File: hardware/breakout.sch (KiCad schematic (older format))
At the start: 4 parts, among them J1 Conn_01x18_Male, J2 Conn_Coaxial, J3 Conn_01x18_Male, U1 RFM95W-915S2

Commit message: Create pcb
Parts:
- added J4: Conn_Coaxial, KiCad/kicad-footprints/Connector_Coaxial.pretty:U.FL_Molex_MCRF_73412-0110_Vertical, symbol Connector:Conn_Coaxial
- added JP1: SolderJumper, KiCad/kicad-footprints/Jumper.pretty:SolderJumper-3_P1.3mm_Open_RoundedPad1.0x1.5mm, symbol Jumper:SolderJumper_3_Open
- J1, J3: footprint (none) -> KiCad/kicad-footprints/Connector_PinHeader_2.54mm.pretty:PinHeader_1x18_P2.54mm_Vertical
- J2: footprint (none) -> KiCad/kicad-footprints/Connector_Coaxial.pretty:SMA_Amphenol_132289_EdgeMount
- U1: footprint (none) -> KiCad/kicad-footprints/RF_Module.pretty:HOPERF_RFM9XW_SMD
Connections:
- net GND: now also J2.2 (Ext), J4.2 (Ext)
- net DIO0: now reaches J3.8 (Pin_8)
- net DIO0: now also U1.14 (DIO0); no longer U1.11 (DIO3)
- net DIO3: now reaches J3.7 (Pin_7)
- net DIO3: now also U1.11 (DIO3); no longer U1.14 (DIO0)
- net at U1.5 (NSS): now also J1.9 (Pin_9)
- net at U1.9 (ANT): now also JP1.2 (C); no longer J2.2 (Ext)
- net at J2.1 (In): now also JP1.1 (A)
- new net: J4.1 (In), JP1.3 (B)
- no-connect marks 28 -> 31
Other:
- moved on the sheet: J2
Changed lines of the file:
@@
 encoding utf-8
 Sheet 1 1
-Title ""
-Date ""
-Rev ""
-Comp ""
+Title "RFM95 Breakout board for Zolertia RE-Mote rev-b"
+Date "2020-10-09"
+Rev "0"
+Comp "Thomas Perale"
 Comment1 ""
 Comment2 ""
@@
 F 0 "U1" H 5900 3950 50  0000 C CNN
 F 1 "RFM95W-915S2" H 6350 3400 50  0000 C CNN
-F 2 "" H 2600 5600 50  0001 C CNN
+F 2 "KiCad/kicad-footprints/RF_Module.pretty:HOPERF_RFM9XW_SMD" H 2600 5600 50  0001 C CNN
 F 3 "https://www.hoperf.com/data/upload/portal/20181127/5bfcbea20e9ef.pdf" H 2600 5600 50  0001 C CNN
 	1    5900 3950
@@
 L Connector:Conn_Coaxial J2
 U 1 1 5F7F506A
-P 6800 2550
-F 0 "J2" H 6900 2525 50  0000 L CNN
-F 1 "Conn_Coaxial" H 6900 2434 50  0000 L CNN
-F 2 "" H 6800 2550 50  0001 C CNN
-F 3 " ~" H 6800 2550 50  0001 C CNN
-	1    6800 2550
-	1    0    0    -1
+P 6150 2800
+F 0 "J2" H 6250 2775 50  0000 L CNN
+F 1 "Conn_Coaxial" H 5600 2500 50  0000 L CNN
+F 2 "KiCad/kicad-footprints/Connector_Coaxial.pretty:SMA_Amphenol_132289_EdgeMount" H 6150 2800 50  0001 C CNN
+F 3 " ~" H 6150 2800 50  0001 C CNN
+	1    6150 2800
+	-1   0    0    1
 $EndComp
 Wire Wire Line
@@
 P 5900 3200
 F 0 "#PWR03" H 5900 3050 50  0001 C CNN
-F 1 "+3.3V" H 5915 3373 50  0000 C CNN
+F 1 "+3.3V" H 5750 3200 50  0000 C CNN
 F 2 "" H 5900 3200 50  0001 C CNN
 F 3 "" H 5900 3200 50  0001 C CNN
@@
 Wire Wire Line
 	5900 3200 5900 3450
-Wire Wire Line
-	6400 3650 6800 3650
-Wire Wire Line
-	6800 3650 6800 2750
 Wire Wire Line
 	4350 4850 4650 4850
@@
 F 0 "J1" H 4258 4931 50  0000 C CNN
 F 1 "Conn_01x18_Male" H 4150 2900 50  0000 C CNN
-F 2 "" H 4150 3950 50  0001 C CNN
+F 2 "KiCad/kicad-footprints/Connector_PinHeader_2.54mm.pretty:PinHeader_1x18_P2.54mm_Vertical" H 4150 3950 50  0001 C CNN
 F 3 "~" H 4150 3950 50  0001 C CNN
 	1    4150 3950
@@
 NoConn ~ 4350 3750
 NoConn ~ 4350 3850
-NoConn ~ 4350 3950
 NoConn ~ 4350 4050
 NoConn ~ 4350 4150
@@
 F 0 "J3" H 7672 3932 50  0000 R CNN
 F 1 "Conn_01x18_Male" H 8000 5000 50  0000 R CNN
-F 2 "" H 7700 4050 50  0001 C CNN
+F 2 "KiCad/kicad-footprints/Connector_PinHeader_2.54mm.pretty:PinHeader_1x18_P2.54mm_Vertical" H 7700 4050 50  0001 C CNN
 F 3 "~" H 7700 4050 50  0001 C CNN
 	1    7700 4050
@@
 NoConn ~ 7500 4850
 NoConn ~ 7500 3250
-Wire Wire Line
-	7500 4150 6900 4150
-Wire Wire Line
-	6900 4150 6900 4050
-Wire Wire Line
-	6900 4050 6400 4050
-Wire Wire Line
-	6900 4250 6900 4350
-Wire Wire Line
-	6900 4350 6400 4350
-Wire Wire Line
-	6900 4250 7500 4250
+NoConn ~ 6400 3850
+NoConn ~ 6400 3950
+NoConn ~ 6400 4150
+NoConn ~ 6400 4250
+$Comp
+L power:GND #PWR0101
+U 1 1 5F81E473
+P 6150 2600
+F 0 "#PWR0101" H 6150 2350 50  0001 C CNN
+F 1 "GND" H 6250 2500 50  0000 C CNN
+F 2 "" H 6150 2600 50  0001 C CNN
+F 3 "" H 6150 2600 50  0001 C CNN
+	1    6150 2600
+	-1   0    0    1
+$EndComp
+Wire Wire Line
+	6400 3650 6550 3650
+Wire Wire Line
+	4350 3950 5400 3950
+Wire Wire Line
+	7500 4250 7350 4250
+Wire Wire Line
+	7500 4150 7350 4150
+Wire Wire Line
+	6400 4050 6650 4050
+Wire Wire Line
+	6400 4350 6650 4350
+Text Label 6650 4350 0    50   ~ 0
+DIO0
+Text Label 7350 4150 2    50   ~ 0
+DIO0
+Text Label 6650 4050 0    50   ~ 0
+DIO3
+Text Label 7350 4250 2    50   ~ 0
+DIO3
+$Comp
+L Connector:Conn_Coaxial J4
+U 1 1 5F844AB1
+P 6950 2800
+F 0 "J4" H 7050 2775 50  0000 L CNN
+F 1 "Conn_Coaxial" H 6950 2950 50  0000 L CNN
+F 2 "KiCad/kicad-footprints/Connector_Coaxial.pretty:U.FL_Molex_MCRF_73412-0110_Vertical" H 6950 2800 50  0001 C CNN
+F 3 " ~" H 6950 2800 50  0001 C CNN
+	1    6950 2800
+	1    0    0    -1
+$EndComp
+$Comp
+L power:GND #PWR0102
+U 1 1 5F8463B3
+P 6950 3000
+F 0 "#PWR0102" H 6950 2750 50  0001 C CNN
+F 1 "GND" H 7050 2900 50  0000 C CNN
+F 2 "" H 6950 3000 50  0001 C CNN
+F 3 "" H 6950 3000 50  0001 C CNN
+	1    6950 3000
+	1    0    0    -1
+$EndComp
+Wire Wire Line
+	6550 2950 6550 3650
+$Comp
+L Jumper:SolderJumper_3_Open JP1
+U 1 1 5F88236B
+P 6550 2800
+F 0 "JP1" H 6550 3005 50  0000 C CNN
+F 1 "SolderJumper" H 6550 2914 50  0000 C CNN
+F 2 "KiCad/kicad-footprints/Jumper.pretty:SolderJumper-3_P1.3mm_Open_RoundedPad1.0x1.5mm" H 6550 2800 50  0001 C CNN
+F 3 "~" H 6550 2800 50  0001 C CNN
+	1    6550 2800
+	1    0    0    -1
+$EndComp
 $EndSCHEMATC

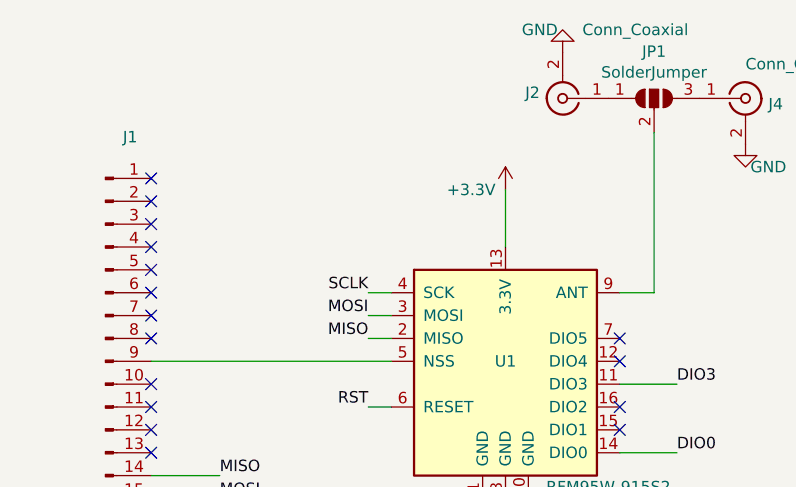
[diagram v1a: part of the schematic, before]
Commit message: [enh] The complete outline is overkill
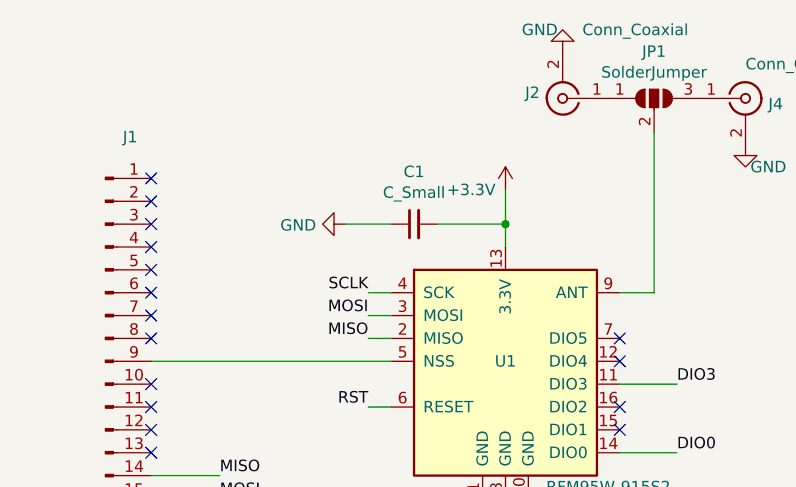
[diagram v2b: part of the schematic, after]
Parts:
- added C1: C_Small, Capacitor_SMD:C_1206_3216Metric_Pad1.33x1.80mm_HandSolder, symbol Device:C_Small
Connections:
- net +3V3: now also C1.2
- net GND: now also C1.1
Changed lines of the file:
@@
 $EndComp
 Wire Wire Line
-	5900 3200 5900 3450
+	5900 3200 5900 3350
 Wire Wire Line
 	4350 4850 4650 4850
@@
 	1    0    0    -1
 $EndComp
+Wire Wire Line
+	5900 3350 5600 3350
+Connection ~ 5900 3350
+Wire Wire Line
+	5900 3350 5900 3450
+$Comp
+L Device:C_Small C1
+U 1 1 5F8492C2
+P 5500 3350
+F 0 "C1" V 5729 3350 50  0000 C CNN
+F 1 "C_Small" V 5638 3350 50  0000 C CNN
+F 2 "Capacitor_SMD:C_1206_3216Metric_Pad1.33x1.80mm_HandSolder" H 5500 3350 50  0001 C CNN
+F 3 "~" H 5500 3350 50  0001 C CNN
+	1    5500 3350
+	0    -1   -1   0
+$EndComp
+Wire Wire Line
+	5400 3350 5200 3350
+$Comp
+L power:GND #PWR0103
+U 1 1 5F84AA53
+P 5200 3350
+F 0 "#PWR0103" H 5200 3100 50  0001 C CNN
+F 1 "GND" V 5205 3222 50  0000 R CNN
+F 2 "" H 5200 3350 50  0001 C CNN
+F 3 "" H 5200 3350 50  0001 C CNN
+	1    5200 3350
+	0    1    1    0
+$EndComp
 $EndSCHEMATC

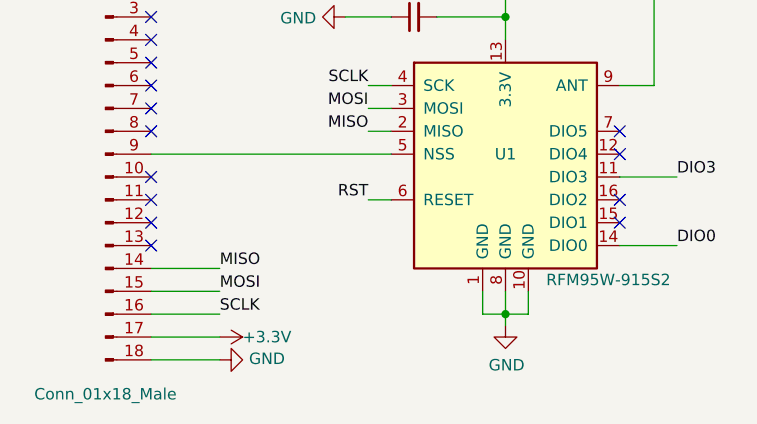
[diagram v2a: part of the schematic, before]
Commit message: [add] Push button for manual rseet
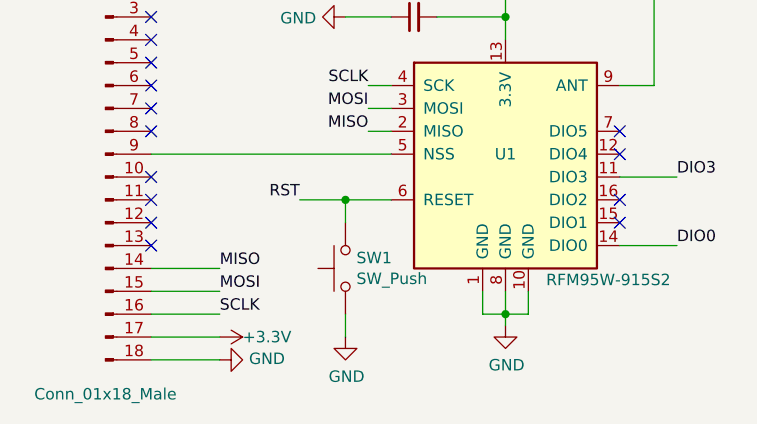
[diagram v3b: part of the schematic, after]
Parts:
- added SW1: SW_Push, KiCad/kicad-footprints/Button_Switch_SMD.pretty:SW_DIP_SPSTx01_Slide_6.7x4.1mm_W8.61mm_P2.54mm_LowProfile, symbol Switch:SW_Push
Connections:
- net GND: now also SW1.1
- net RST: now also SW1.2
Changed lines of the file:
@@
 Text Label 7350 3350 2    50   ~ 0
 RST
-Wire Wire Line
-	5400 4150 5300 4150
-Text Label 5300 4150 2    50   ~ 0
+Text Label 5000 4150 2    50   ~ 0
 RST
 $Comp
@@
 	0    1    1    0
 $EndComp
+Wire Wire Line
+	5000 4150 5200 4150
+Wire Wire Line
+	5200 4150 5200 4250
+Connection ~ 5200 4150
+Wire Wire Line
+	5200 4150 5400 4150
+$Comp
+L Switch:SW_Push SW1
+U 1 1 5F866186
+P 5200 4450
+F 0 "SW1" V 5246 4402 50  0000 R CNN
+F 1 "SW_Push" V 5155 4402 50  0000 R CNN
+F 2 "KiCad/kicad-footprints/Button_Switch_SMD.pretty:SW_DIP_SPSTx01_Slide_6.7x4.1mm_W8.61mm_P2.54mm_LowProfile" H 5200 4650 50  0001 C CNN
+F 3 "~" H 5200 4650 50  0001 C CNN
+	1    5200 4450
+	0    -1   -1   0
+$EndComp
+Wire Wire Line
+	5200 4650 5200 4750
+$Comp
+L power:GND #PWR0104
+U 1 1 5F867EB7
+P 5200 4750
+F 0 "#PWR0104" H 5200 4500 50  0001 C CNN
+F 1 "GND" H 5205 4577 50  0000 C CNN
+F 2 "" H 5200 4750 50  0001 C CNN
+F 3 "" H 5200 4750 50  0001 C CNN
+	1    5200 4750
+	1    0    0    -1
+$EndComp
 $EndSCHEMATC

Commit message: [add] Debouncing circuit
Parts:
- added C2: 1uF, Capacitor_SMD:C_1206_3216Metric_Pad1.33x1.80mm_HandSolder, symbol Device:C_Small
- added R1: 220R, Resistor_SMD:R_1206_3216Metric_Pad1.30x1.75mm_HandSolder, symbol Device:R_Small
- added R2: 10KR, Resistor_SMD:R_1206_3216Metric_Pad1.30x1.75mm_HandSolder, symbol Device:R_Small
- C1: value C_Small -> 10uF
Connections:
- net +3V3: now also R2.2
- net GND: now also C2.1
- net RST: now also C2.2, R1.2; no longer J3.16 (Pin_16), SW1.2
- new net RST_GPIO: J3.16 (Pin_16), R1.1, R2.1, SW1.2
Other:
- note added: "Reset Push Button"
- moved on the sheet: SW1
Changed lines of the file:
@@
 	7500 3350 7350 3350
 Text Label 7350 3350 2    50   ~ 0
-RST
-Text Label 5000 4150 2    50   ~ 0
+RST_GPIO
+Text Label 5300 4150 2    50   ~ 0
 RST
 $Comp
@@
 P 5500 3350
 F 0 "C1" V 5729 3350 50  0000 C CNN
-F 1 "C_Small" V 5638 3350 50  0000 C CNN
+F 1 "10uF" V 5638 3350 50  0000 C CNN
 F 2 "Capacitor_SMD:C_1206_3216Metric_Pad1.33x1.80mm_HandSolder" H 5500 3350 50  0001 C CNN
 F 3 "~" H 5500 3350 50  0001 C CNN
@@
 	0    1    1    0
 $EndComp
-Wire Wire Line
-	5000 4150 5200 4150
-Wire Wire Line
-	5200 4150 5200 4250
-Connection ~ 5200 4150
-Wire Wire Line
-	5200 4150 5400 4150
 $Comp
 L Switch:SW_Push SW1
 U 1 1 5F866186
-P 5200 4450
-F 0 "SW1" V 5246 4402 50  0000 R CNN
-F 1 "SW_Push" V 5155 4402 50  0000 R CNN
-F 2 "KiCad/kicad-footprints/Button_Switch_SMD.pretty:SW_DIP_SPSTx01_Slide_6.7x4.1mm_W8.61mm_P2.54mm_LowProfile" H 5200 4650 50  0001 C CNN
-F 3 "~" H 5200 4650 50  0001 C CNN
-	1    5200 4450
+P 2300 4300
+F 0 "SW1" V 2250 4250 50  0000 R CNN
+F 1 "SW_Push" V 2150 4250 50  0000 R CNN
+F 2 "KiCad/kicad-footprints/Button_Switch_SMD.pretty:SW_DIP_SPSTx01_Slide_6.7x4.1mm_W8.61mm_P2.54mm_LowProfile" H 2300 4500 50  0001 C CNN
+F 3 "~" H 2300 4500 50  0001 C CNN
+	1    2300 4300
 	0    -1   -1   0
 $EndComp
-Wire Wire Line
-	5200 4650 5200 4750
 $Comp
 L power:GND #PWR0104
 U 1 1 5F867EB7
-P 5200 4750
-F 0 "#PWR0104" H 5200 4500 50  0001 C CNN
-F 1 "GND" H 5205 4577 50  0000 C CNN
-F 2 "" H 5200 4750 50  0001 C CNN
-F 3 "" H 5200 4750 50  0001 C CNN
-	1    5200 4750
-	1    0    0    -1
-$EndComp
+P 2300 4800
+F 0 "#PWR0104" H 2300 4550 50  0001 C CNN
+F 1 "GND" H 2305 4627 50  0000 C CNN
+F 2 "" H 2300 4800 50  0001 C CNN
+F 3 "" H 2300 4800 50  0001 C CNN
+	1    2300 4800
+	1    0    0    -1
+$EndComp
+Wire Wire Line
+	2000 4000 2000 4200
+$Comp
+L Device:C_Small C2
+U 1 1 5F874ED2
+P 2000 4300
+F 0 "C2" H 1950 4400 50  0000 C CNN
+F 1 "1uF" H 1900 4500 50  0000 C CNN
+F 2 "Capacitor_SMD:C_1206_3216Metric_Pad1.33x1.80mm_HandSolder" H 2000 4300 50  0001 C CNN
+F 3 "~" H 2000 4300 50  0001 C CNN
+	1    2000 4300
+	-1   0    0    1
+$EndComp
+Wire Wire Line
+	2000 4400 2000 4650
+Wire Wire Line
+	2000 4650 2300 4650
+Wire Wire Line
+	5300 4150 5400 4150
+Wire Wire Line
+	2300 4500 2300 4650
+Connection ~ 2300 4650
+Wire Wire Line
+	2300 4650 2300 4800
+Wire Wire Line
+	2300 4100 2300 4000
+Wire Wire Line
+	2300 4000 2550 4000
+$Comp
+L Device:R_Small R1
+U 1 1 5F8A20C0
+P 2150 4000
+F 0 "R1" V 1954 4000 50  0000 C CNN
+F 1 "220R" V 2045 4000 50  0000 C CNN
+F 2 "Resistor_SMD:R_1206_3216Metric_Pad1.30x1.75mm_HandSolder" H 2150 4000 50  0001 C CNN
+F 3 "~" H 2150 4000 50  0001 C CNN
+	1    2150 4000
+	0    1    1    0
+$EndComp
+Wire Wire Line
+	2250 4000 2300 4000
+Connection ~ 2300 4000
+Wire Wire Line
+	2050 4000 2000 4000
+Connection ~ 2000 4000
+Wire Wire Line
+	1700 4000 2000 4000
+Text Label 2550 4000 0    50   ~ 0
+RST_GPIO
+$Comp
+L Device:R_Small R2
+U 1 1 5F8A648B
+P 2300 3650
+F 0 "R2" H 2241 3604 50  0000 R CNN
+F 1 "10KR" H 2241 3695 50  0000 R CNN
+F 2 "Resistor_SMD:R_1206_3216Metric_Pad1.30x1.75mm_HandSolder" H 2300 3650 50  0001 C CNN
+F 3 "~" H 2300 3650 50  0001 C CNN
+	1    2300 3650
+	-1   0    0    1
+$EndComp
+Wire Wire Line
+	2300 4000 2300 3750
+Wire Wire Line
+	2300 3550 2300 3400
+$Comp
+L power:+3.3V #PWR05
+U 1 1 5F8ACC15
+P 2300 3400
+F 0 "#PWR05" H 2300 3250 50  0001 C CNN
+F 1 "+3.3V" V 2300 3500 50  0000 L CNN
+F 2 "" H 2300 3400 50  0001 C CNN
+F 3 "" H 2300 3400 50  0001 C CNN
+	1    2300 3400
+	1    0    0    -1
+$EndComp
+Text Label 1700 4000 2    50   ~ 0
+RST
+Wire Notes Line
+	1450 5050 1450 3000
+Wire Notes Line
+	1450 3000 3000 3000
+Wire Notes Line
+	3000 3000 3000 5050
+Wire Notes Line
+	3000 5050 1450 5050
+Text Notes 1450 3000 0    50   ~ 0
+Reset Push Button
 $EndSCHEMATC

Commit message: [fix] fixed board size + 3v3 input + reset button
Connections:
- net +3V3: now also J3.3 (Pin_3); no longer J1.17 (Pin_17)
- net RST_GPIO: now also J1.1 (Pin_1); no longer J3.16 (Pin_16)
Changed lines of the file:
@@
 $EndComp
 Wire Wire Line
-	4350 4750 4650 4750
+	7500 4650 7200 4650
 $Comp
 L power:+3.3V #PWR01
 U 1 1 5F80DD51
-P 4650 4750
-F 0 "#PWR01" H 4650 4600 50  0001 C CNN
-F 1 "+3.3V" V 4650 4850 50  0000 L CNN
-F 2 "" H 4650 4750 50  0001 C CNN
-F 3 "" H 4650 4750 50  0001 C CNN
-	1    4650 4750
-	0    1    1    0
+P 7200 4650
+F 0 "#PWR01" H 7200 4500 50  0001 C CNN
+F 1 "+3.3V" V 7200 4750 50  0000 L CNN
+F 2 "" H 7200 4650 50  0001 C CNN
+F 3 "" H 7200 4650 50  0001 C CNN
+	1    7200 4650
+	0    -1   -1   0
 $EndComp
 $Comp
@@
 Text Label 5300 3850 2    50   ~ 0
 MISO
-NoConn ~ 4350 3150
+NoConn ~ 7500 3650
 NoConn ~ 4350 3250
 NoConn ~ 4350 3350
@@
 NoConn ~ 4350 4350
 Wire Wire Line
-	7500 3350 7350 3350
-Text Label 7350 3350 2    50   ~ 0
+	4350 3150 4500 3150
+Text Label 4500 3150 0    50   ~ 0
 RST_GPIO
 Text Label 5300 4150 2    50   ~ 0
@@
 NoConn ~ 7500 3450
 NoConn ~ 7500 3550
-NoConn ~ 7500 3650
+NoConn ~ 7500 3350
 NoConn ~ 7500 3750
 NoConn ~ 7500 3850
@@
 NoConn ~ 7500 4450
 NoConn ~ 7500 4550
-NoConn ~ 7500 4650
+NoConn ~ 4350 4750
 NoConn ~ 7500 4750
 NoConn ~ 7500 4850

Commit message: fix the footprint of the antenna connector
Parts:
- J2: footprint KiCad/kicad-footprints/Connector_Coaxial.pretty:SMA_Amphenol_132289_EdgeMount -> KiCad/kicad-footprints/Connector_Coaxial.pretty:SMA_Samtec_SMA-J-P-X-ST-EM1_EdgeMount
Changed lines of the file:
@@
 F 0 "J2" H 6250 2775 50  0000 L CNN
 F 1 "Conn_Coaxial" H 5600 2500 50  0000 L CNN
-F 2 "KiCad/kicad-footprints/Connector_Coaxial.pretty:SMA_Amphenol_132289_EdgeMount" H 6150 2800 50  0001 C CNN
+F 2 "KiCad/kicad-footprints/Connector_Coaxial.pretty:SMA_Samtec_SMA-J-P-X-ST-EM1_EdgeMount" H 6150 2800 50  0001 C CNN
 F 3 " ~" H 6150 2800 50  0001 C CNN
 	1    6150 2800
